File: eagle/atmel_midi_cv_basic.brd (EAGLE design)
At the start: 101 x 82 mm, 42 parts, among them IC1 TL074P, Q2 2N3904, U1 ATMEGA328P_PDIP

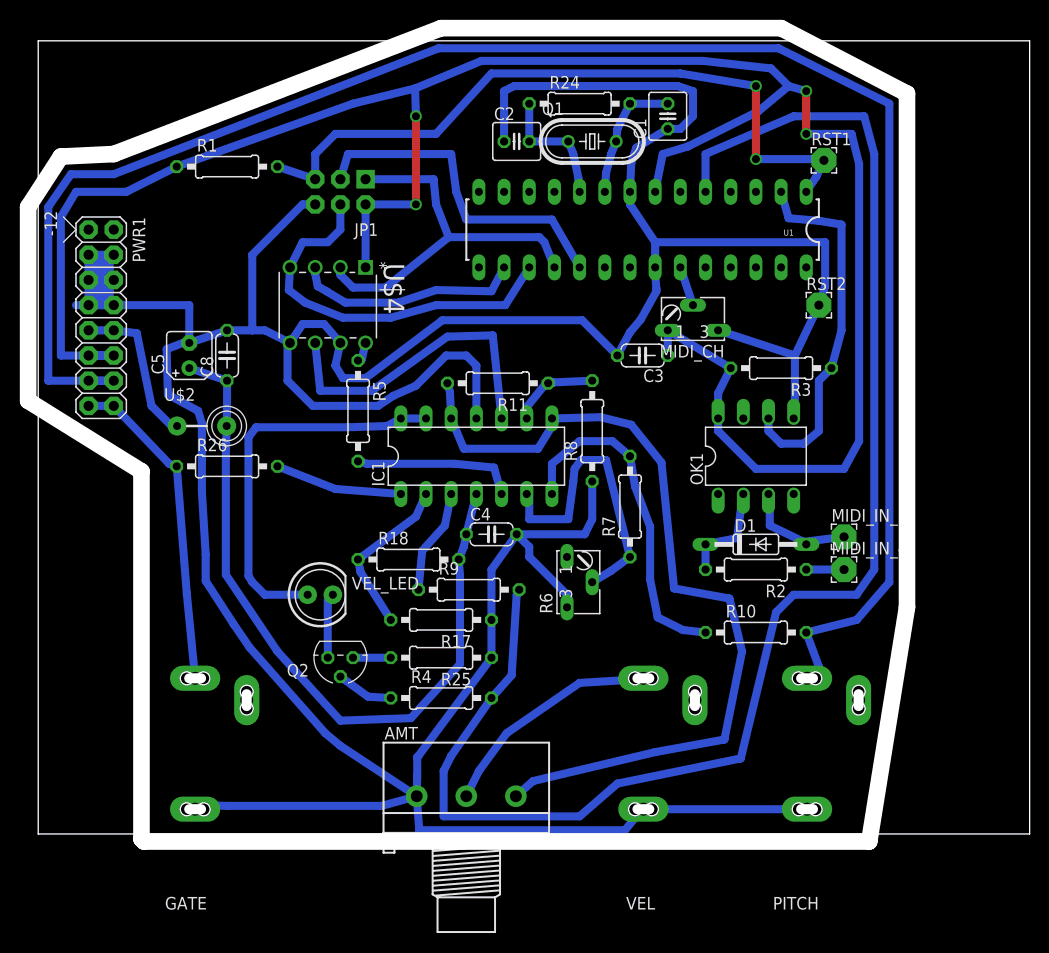
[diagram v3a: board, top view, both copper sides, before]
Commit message: swapping atmega pin 16 and 17 for layout convenience
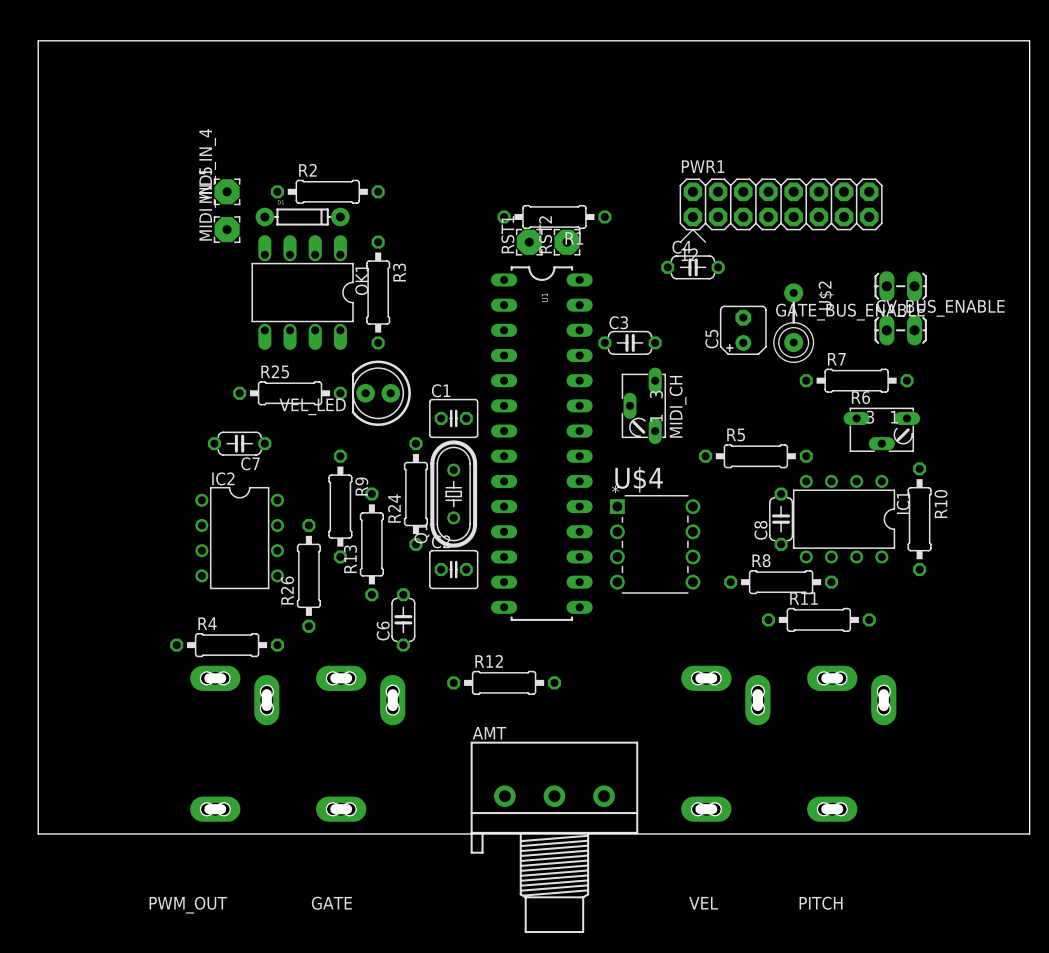
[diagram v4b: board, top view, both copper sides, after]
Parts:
- removed JP1: (no value), SparkFun-Connectors:2X3-NS
- removed Q2: 2N3904, transistor-npn:TO92
- removed R17: 10k, rcl:0207/10
- removed R18: 47k, rcl:0207/10
- added C6, C7: 100n, rcl:C050-024X044
- added CV_BUS_ENABLE, GATE_BUS_ENABLE: M02LOCK_LONGPADS, SparkFun-Connectors:1X02_LOCK_LONGPADS
- added IC2: TL072P, linear:DIL08
- added PWM_OUT: AUDIO-JACK, erthenvar:ERTHENVAR-JACK-90DEG
- added R12: 3k9, rcl:0207/10
- added R13: 1k, rcl:0207/10
- D1: value 1N4148DO35-10 -> (none); device diode:DO35-10 -> SparkFun-DiscreteSemi:DIODE-1N4148
- IC1: value TL074P -> TL072P; device linear:DIL14 -> linear:DIL08
- R4: value 3k3 -> 1k
- R9: value 1k -> 1k5
- moved MIDI_IN_4 73.0 mm to (19.1, 64.8), turned to 90 degrees
- moved MIDI_IN_5 69.5 mm to (19.1, 61.0), turned to 90 degrees
- moved PWR1 66.6 mm to (72.4, 63.5), turned to 0 degrees
- moved U$2 60.7 mm to (76.2, 52.1), turned to 270 degrees
- moved C8 58.3 mm to (74.9, 31.8)
- moved R2 57.6 mm to (29.2, 64.8), turned to 0 degrees
- moved D1 56.4 mm to (26.7, 62.2)
- moved C5 55.9 mm to (71.1, 50.8)
- moved OK1 48.6 mm to (26.7, 54.6), turned to 180 degrees
- moved U$4 47.3 mm to (66.0, 25.4), turned to 0 degrees
- moved C2 43.6 mm to (41.9, 26.7)
- moved R24 42.7 mm to (38.1, 34.3), turned to 90 degrees
- moved R3 41.3 mm to (34.3, 54.6), turned to 270 degrees
- moved R5 40.4 mm to (72.4, 38.1), turned to 0 degrees
- moved R11 40.2 mm to (78.7, 21.6), turned to 0 degrees
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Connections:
- new net N$18: R25.2, VEL_LED.K
- new net N$28: C6.1, IC2.3, R12.1
- net +12V: now also C7.1, IC1.8, IC2.8; no longer IC1.4, R18.2
- net +5V: no longer JP1.2
- net GND: now also C6.2, C7.2, IC1.4, IC2.4, PWM_OUT.P$1, R13.2; no longer IC1.11, JP1.6, R17.1
- net N$1: now also GATE_BUS_ENABLE.2, PWR1.15, PWR1.16; no longer IC1.3, R9.1
- net N$10: now also IC2.6, R13.1, R9.2; no longer JP1.3, U1.19
- net N$12: now also IC1.2; no longer IC1.6
- net N$13: now also IC1.6; no longer IC1.9
- net N$14: now also IC1.5; no longer IC1.10
- net N$15: now also CV_BUS_ENABLE.1, PWR1.13, PWR1.14; no longer IC1.2, R17.2, R18.1
- net N$16: now also IC2.7, R9.1; no longer IC1.1
- net N$17: now also IC1.7; no longer IC1.12, IC1.8
- net N$20: now also U1.6, VEL_LED.A; no longer Q2.1, VEL_LED.K
- net N$21: now also R12.2, U1.11; no longer IC1.13, IC1.14, VEL_LED.A
- net N$22: now also IC2.5; no longer R4.2, R9.2
- net N$23: now also IC2.1, IC2.2; no longer Q2.2
- net N$24: now also PWM_OUT.P$3, R4.2; no longer Q2.3, R25.2
- net N$25: now also U1.17; no longer U1.16
- net N$26: now also U1.16; no longer JP1.4, U1.17
- net N$27: now also IC1.1; no longer IC1.7
- net N$31: now also GATE_BUS_ENABLE.1; no longer PWR1.15, PWR1.16
- net N$43: no longer JP1.5
- net N$45: no longer JP1.1
- net N$6: now also IC1.3; no longer IC1.5
- net N$9: now also CV_BUS_ENABLE.2; no longer PWR1.13, PWR1.14
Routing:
- net GND: track 406.0 -> 0.00 mm
- net +5V: track 217.4 -> 0.00 mm, vias 4 -> 0
- net N$9: track 180.8 -> 0.00 mm
- net N$22: track 150.2 -> 0.00 mm
- net N$17: track 86.0 -> 0.00 mm
- net +12V: track 74.2 -> 0.00 mm
- net N$43: track 72.6 -> 0.00 mm, vias 2 -> 0
- net N$45: track 39.5 -> 0.00 mm
- net N$21: track 39.4 -> 0.00 mm
- net N$26: track 39.3 -> 0.00 mm
- net N$30: track 37.0 -> 0.00 mm
- net N$10: track 34.1 -> 0.00 mm
- net N$27: track 34.1 -> 0.00 mm
- net N$31: track 32.9 -> 0.00 mm
- net N$14: track 32.4 -> 0.00 mm
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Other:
- board size 101 x 82 mm -> 100 x 80 mm

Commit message: possible route
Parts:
- removed R6: 10k, pot:B64W
- added SCALE_TRIM: 10k, pot:B64W
- moved MIDI_IN_4 20.8 mm to (35.6, 52.1), turned to 270 degrees
- moved MIDI_IN_5 17.3 mm to (35.6, 55.9), turned to 270 degrees
- moved R3 15.3 mm to (20.3, 61.0), turned to 90 degrees
- moved R2 14.2 mm to (26.7, 50.8), turned to 180 degrees
- moved C6 13.7 mm to (41.9, 8.89), turned to 270 degrees
- moved D1 8.98 mm to (27.9, 53.3), turned to 180 degrees
- moved R4 7.38 mm to (14.2, 24.6), turned to 270 degrees
- moved OK1 6.48 mm to (27.9, 61.0), turned to 0 degrees
- moved R12 6.27 mm to (43.3, 20.3), turned to 90 degrees
- moved VEL_LED 5.80 mm to (39.6, 46.7)
- moved R25 5.11 mm to (30.5, 43.9)
- moved C4 4.02 mm to (67.3, 53.3), turned to 90 degrees
- moved C8 3.81 mm to (71.1, 31.8), turned to 270 degrees
- moved R10 3.57 mm to (85.3, 31.5)
- moved R7 2.65 mm to (81.8, 43.2), turned to 270 degrees
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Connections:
- removed net GND: AMT.1, C1.1, C2.1, C3.2, C4.2, C5.-, C6.2, C7.2, C8.2, GATE.P$1, IC1.4, IC2.4, MIDI_CH.E, OK1.5, PITCH.P$1, PWM_OUT.P$1, PWR1.3, PWR1.4, PWR1.5, PWR1.6, PWR1.7, PWR1.8, R13.2, R25.1, R6.E, R8.1, RST2.1, U$4.5, U$4.7, U1.22, U1.8, VEL.P$1
- new net N$29: AMT.1, C1.1, C2.1, C3.2, C4.2, C5.-, C6.2, C7.2, C8.2, GATE.P$1, IC1.4, IC2.4, MIDI_CH.A, OK1.5, PITCH.P$1, PWM_OUT.P$1, PWR1.3, PWR1.4, PWR1.5, PWR1.6, PWR1.7, PWR1.8, R13.2, R25.1, R8.1, RST2.1, SCALE_TRIM.E, U$4.5, U$4.7, U1.22, U1.8, VEL.P$1
- net +5V: now also MIDI_CH.E; no longer MIDI_CH.A
- net N$12: now also SCALE_TRIM.S; no longer R6.S
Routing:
- net N$29: track 0.00 -> 375.6 mm
- net +5V: track 0.00 -> 187.3 mm
- net +12V: track 0.00 -> 159.4 mm
- net N$31: track 0.00 -> 155.0 mm
- net N$22: track 0.00 -> 51.8 mm, vias 0 -> 2
- net N$17: track 0.00 -> 46.2 mm
- net N$9: track 0.00 -> 39.5 mm
- net N$30: track 0.00 -> 36.3 mm
- net N$28: track 0.00 -> 35.7 mm
- net N$51: track 0.00 -> 25.5 mm
- net N$12: track 0.00 -> 18.6 mm
- net N$15: track 0.00 -> 15.8 mm
- net N$4: track 0.00 -> 15.2 mm
- net N$5: track 0.00 -> 13.4 mm
- net N$3: track 0.00 -> 11.2 mm
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
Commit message: routed
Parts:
- moved R25 4.58 mm to (34.3, 41.4), turned to 90 degrees
- moved R4 4.54 mm to (18.3, 22.6), turned to 180 degrees
- moved PWR1 2.54 mm to (69.8, 63.5)
- moved R9 2.03 mm to (29.2, 30.2)
- moved C8 1.98 mm to (69.8, 30.2)
- moved C7 1.78 mm to (20.3, 37.6)
- moved R11 1.52 mm to (74.9, 21.6)
- moved VEL_LED 1.05 mm to (39.4, 47.8)
- moved C1 0.76 mm to (39.9, 41.9)
- moved R13 0.72 mm to (33.1, 28.7)
- moved U$2 0.51 mm to (75.7, 52.1)
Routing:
- net N$29: track 375.6 -> 352.0 mm
- net +12V: track 159.4 -> 145.9 mm, vias 0 -> 2
- net N$17: track 46.2 -> 57.6 mm
- net N$23: track 5.43 -> 14.1 mm
- net +5V: track 187.3 -> 179.9 mm
- net N$31: track 155.0 -> 148.0 mm
- net N$28: track 35.7 -> 39.6 mm
- net N$51: track 25.5 -> 28.4 mm
- net N$24: track 5.66 -> 8.57 mm
- net N$4: track 15.2 -> 13.1 mm
- net N$13: track 10.8 -> 12.7 mm
- net N$14: track 9.31 -> 11.1 mm
- net N$16: track 10.4 -> 8.63 mm
- net N$19: track 8.09 -> 6.61 mm
- net N$3: track 11.2 -> 9.72 mm
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
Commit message: new gcode
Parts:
- moved RST2 9.67 mm to (44.5, 63.5)
- moved RST1 5.08 mm to (44.5, 59.7)
- moved R1 4.02 mm to (52.1, 59.7)
- moved R3 1.27 mm to (20.3, 59.7)
- moved PWR1 1.27 mm to (68.6, 63.5)
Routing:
- net N$29: track 352.0 -> 346.9 mm
- net +5V: track 179.9 -> 176.7 mm
- net N$43: track 10.3 -> 7.40 mm
- net N$30: track 36.5 -> 37.7 mm
- net N$11: track 10.5 -> 11.2 mm
- net N$31: track 148.0 -> 147.2 mm
- net N$15: track 15.8 -> 16.3 mm
- net N$1: track 10.5 -> 11.0 mm
- net N$12: track 18.6 -> 18.1 mm
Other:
- board size 100 x 80 mm -> 100 x 80.8 mm

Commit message: layout tweaked
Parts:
- moved R10 11.7 mm to (84.3, 43.2), turned to 90 degrees
- moved R13 3.53 mm to (34.9, 25.7)
- moved GATE_BUS_ENABLE 2.84 mm to (84.5, 56.5)
- moved CV_BUS_ENABLE 2.65 mm to (81.9, 51.6)
- moved R9 1.98 mm to (30.5, 28.7)
- moved R7 0.76 mm to (81.0, 43.2)
- moved R26 0.25 mm to (27.1, 25.7)
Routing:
- net N$9: track 39.3 -> 42.8 mm
- net N$31: track 147.2 -> 144.0 mm
- net N$10: track 10.5 -> 13.6 mm
- net N$1: track 11.0 -> 8.57 mm
- net N$15: track 16.3 -> 15.2 mm
- net +12V: track 145.8 -> 144.9 mm
- net N$12: track 18.1 -> 17.5 mm
- net N$16: track 8.63 -> 8.03 mm
- net N$3: track 9.72 -> 10.3 mm
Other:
- outline, holes or cut-outs redrawn
